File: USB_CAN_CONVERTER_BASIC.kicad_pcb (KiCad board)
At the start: 2 copper layers, 26.6 x 14.9 mm, 24 parts, among them P1 CONN_01X05, P2 CONN_01X02, P3 USB_A, P4 CONN_01X04, U1 STM32F042C6Ux, U2 PSD2CAN, U3 SN65HVD232D, U4 MCP1700T-3302E/TT, U5 USBLC6-2

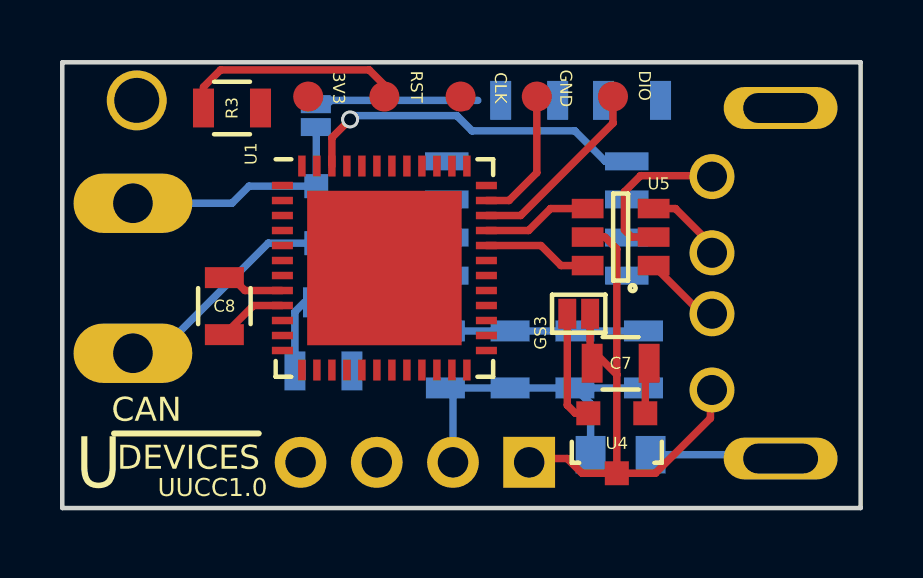
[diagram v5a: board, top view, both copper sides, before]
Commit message: USART change
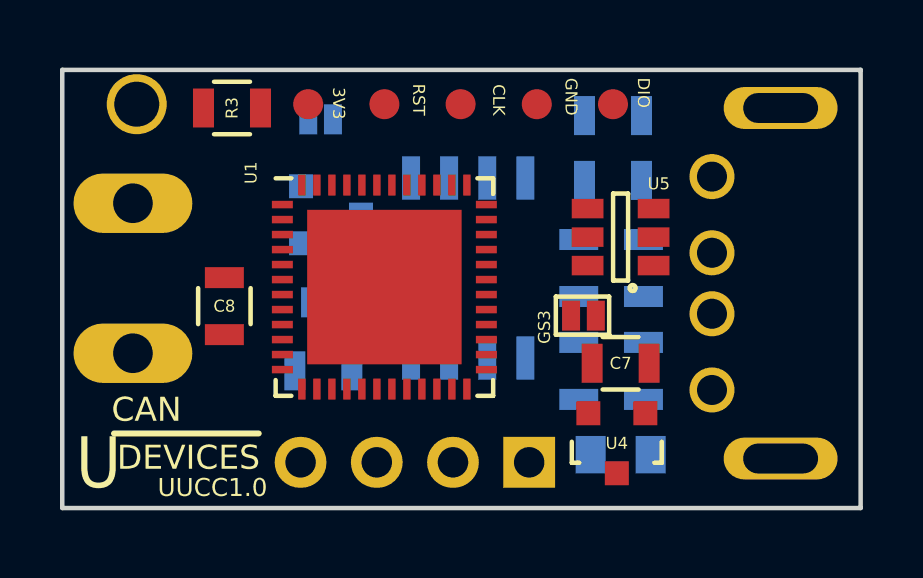
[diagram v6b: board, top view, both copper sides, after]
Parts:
- moved C3 5.39 mm to (157.6, 98.7), turned to 90 degrees
- moved C5 5.39 mm to (159.8, 98.7), turned to 90 degrees
- moved R4 3.86 mm to (158.8, 95.8), turned to 180 degrees
- moved U3 2.82 mm to (153.9, 98.7), turned to 270 degrees
- moved C1 0.81 mm to (158.8, 93.6)
- moved U1 0.63 mm to (151.1, 99.3)
- moved U2 0.51 mm to (149.4, 96.9)
- moved C4 0.40 mm to (157.6, 102.1)
- moved C2 0.38 mm to (159.8, 102.1)
- moved P1 0.25 mm to (152.4, 93.2)
- moved GS1 0.18 mm to (149.0, 93.7), turned to 90 degrees
- moved GS3 0.14 mm to (157.7, 100.3)
- moved REF** 0.13 mm to (142.9, 93.2)
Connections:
- P4 pad 3: /USART1_TX -> /USART_TX
- P4 pad 4: /USART1_RX -> /USART_RX
- U1 pad 1: Net-(U1-Pad1) -> (no net)
- U1 pad 10: Net-(U1-Pad10) -> (no net)
- U1 pad 11: Net-(U1-Pad11) -> (no net)
- U1 pad 12: Net-(U1-Pad12) -> /USART_TX
- U1 pad 13: Net-(U1-Pad13) -> /USART_RX
- U1 pad 14: Net-(U1-Pad14) -> (no net)
- U1 pad 15: Net-(U1-Pad15) -> (no net)
- U1 pad 16: Net-(U1-Pad16) -> (no net)
- U1 pad 17: Net-(U1-Pad17) -> (no net)
- U1 pad 18: Net-(U1-Pad18) -> (no net)
- U1 pad 19: Net-(U1-Pad19) -> (no net)
- U1 pad 2: Net-(U1-Pad2) -> (no net)
- U1 pad 20: Net-(U1-Pad20) -> (no net)
- U1 pad 21: Net-(U1-Pad21) -> (no net)
- U1 pad 22: Net-(U1-Pad22) -> (no net)
- U1 pad 25: Net-(U1-Pad25) -> (no net)
- U1 pad 26: Net-(U1-Pad26) -> (no net)
- U1 pad 27: Net-(U1-Pad27) -> (no net)
- U1 pad 28: Net-(U1-Pad28) -> (no net)
- U1 pad 29: Net-(U1-Pad29) -> (no net)
- U1 pad 3: Net-(U1-Pad3) -> (no net)
- U1 pad 30: /USART1_TX -> (no net)
- U1 pad 31: /USART1_RX -> (no net)
- U1 pad 38: Net-(U1-Pad38) -> (no net)
- U1 pad 39: Net-(U1-Pad39) -> (no net)
- U1 pad 4: Net-(U1-Pad4) -> (no net)
- U1 pad 40: Net-(U1-Pad40) -> (no net)
- U1 pad 41: Net-(U1-Pad41) -> (no net)
- U1 pad 42: Net-(U1-Pad42) -> (no net)
- U1 pad 43: Net-(U1-Pad43) -> (no net)
- U1 pad 44: Net-(U1-Pad44) -> (no net)
- U1 pad 6: Net-(U1-Pad6) -> (no net)
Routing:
- net GND: track 25.7 -> 0.00 mm
- net +5V: track 19.5 -> 0.00 mm
- net +3V3: track 12.6 -> 0.00 mm
- net CAN_TX: track 11.7 -> 0.00 mm, vias 1 -> 0
- net Net-(GS2-Pad2): track 10.0 -> 0.00 mm
- net Net-(GS1-Pad2): track 8.18 -> 0.00 mm
- net Net-(P1-Pad2): track 7.69 -> 0.00 mm
- net SW_DIO: track 6.26 -> 0.00 mm
- net Net-(GS1-Pad1): track 5.45 -> 0.00 mm
- net Net-(L1-Pad2): track 4.32 -> 0.00 mm
- net Net-(U1-Pad33): track 3.68 -> 0.00 mm
- net Net-(U1-Pad32): track 3.65 -> 0.00 mm
- net Net-(P3-Pad3): track 2.65 -> 0.00 mm
- net Net-(P3-Pad2): track 2.55 -> 0.00 mm
- net Net-(GS2-Pad1): track 2.42 -> 0.00 mm
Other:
- board size 26.6 x 14.9 mm -> 26.6 x 14.6 mm

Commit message: Board rooting done.
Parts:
- moved C5 8.56 mm to (151.9, 102.2), turned to 270 degrees
- moved R4 7.09 mm to (152.1, 93.3), turned to 0 degrees
- moved C3 4.89 mm to (154.2, 102.2), turned to 270 degrees
- moved U3 2.69 mm to (156.3, 97.4), turned to 180 degrees
- moved R3 2.36 mm to (145.9, 95.7), turned to 90 degrees
- moved C1 1.30 mm to (157.5, 93.3)
- moved C8 1.25 mm to (145.8, 101.2)
- moved GS3 0.46 mm to (157.3, 100.3)
- moved U2 0.45 mm to (149.0, 97.2), turned to 270 degrees
- moved U5 0.42 mm to (158.7, 97.9)
- moved GS1 0.42 mm to (148.7, 93.4)
- moved P1 0.15 mm to (152.4, 93.4)
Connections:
- REF** pad 1: (no net) -> GND
- U1 pad 1: (no net) -> Net-(U1-Pad1)
- U1 pad 10: (no net) -> Net-(U1-Pad10)
- U1 pad 11: (no net) -> Net-(U1-Pad11)
- U1 pad 14: (no net) -> Net-(U1-Pad14)
- U1 pad 15: (no net) -> Net-(U1-Pad15)
- U1 pad 16: (no net) -> Net-(U1-Pad16)
- U1 pad 17: (no net) -> Net-(U1-Pad17)
- U1 pad 18: (no net) -> Net-(U1-Pad18)
- U1 pad 19: (no net) -> Net-(U1-Pad19)
- U1 pad 2: (no net) -> Net-(U1-Pad2)
- U1 pad 20: (no net) -> Net-(U1-Pad20)
- U1 pad 21: (no net) -> Net-(U1-Pad21)
- U1 pad 22: (no net) -> Net-(U1-Pad22)
- U1 pad 25: (no net) -> Net-(U1-Pad25)
- U1 pad 26: (no net) -> Net-(U1-Pad26)
- U1 pad 27: (no net) -> Net-(U1-Pad27)
- U1 pad 28: (no net) -> Net-(U1-Pad28)
- U1 pad 29: (no net) -> Net-(U1-Pad29)
- U1 pad 3: (no net) -> Net-(U1-Pad3)
- U1 pad 30: (no net) -> Net-(U1-Pad30)
- U1 pad 31: (no net) -> Net-(U1-Pad31)
- U1 pad 38: (no net) -> Net-(U1-Pad38)
- U1 pad 39: (no net) -> Net-(U1-Pad39)
- U1 pad 4: (no net) -> Net-(U1-Pad4)
- U1 pad 40: (no net) -> Net-(U1-Pad40)
- U1 pad 41: (no net) -> Net-(U1-Pad41)
- U1 pad 42: (no net) -> Net-(U1-Pad42)
- U1 pad 43: (no net) -> Net-(U1-Pad43)
- U1 pad 44: (no net) -> Net-(U1-Pad44)
- U1 pad 6: (no net) -> Net-(U1-Pad6)
- U2 pad 1: Net-(GS2-Pad2) -> Net-(GS1-Pad2)
- U2 pad 2: Net-(GS1-Pad2) -> Net-(GS2-Pad2)
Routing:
- net GND: track 0.00 -> 105.3 mm, vias 0 -> 1
- net +3V3: track 0.00 -> 53.9 mm, vias 0 -> 5
- net Net-(C1-Pad2): track 0.00 -> 32.0 mm, vias 0 -> 2
- net CAN_MOD: track 0.00 -> 18.5 mm, vias 0 -> 1
- net +5V: track 0.00 -> 17.9 mm
- net Net-(GS2-Pad2): track 0.00 -> 16.7 mm
- net Net-(L1-Pad2): track 0.00 -> 16.0 mm
- net Net-(GS1-Pad2): track 0.00 -> 14.6 mm
- net Net-(P1-Pad2): track 0.00 -> 14.3 mm
- net CAN_RX: track 0.00 -> 12.3 mm, vias 0 -> 1
- net CAN_TX: track 0.00 -> 11.5 mm, vias 0 -> 1
- net /USART_TX: track 0.00 -> 9.65 mm
- net SW_DIO: track 0.00 -> 6.44 mm
- net Net-(U1-Pad33): track 0.00 -> 3.51 mm
- net Net-(U1-Pad32): track 0.00 -> 3.21 mm
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- added copper zone on B.Cu, net GND
- added copper zone on F.Cu, net GND

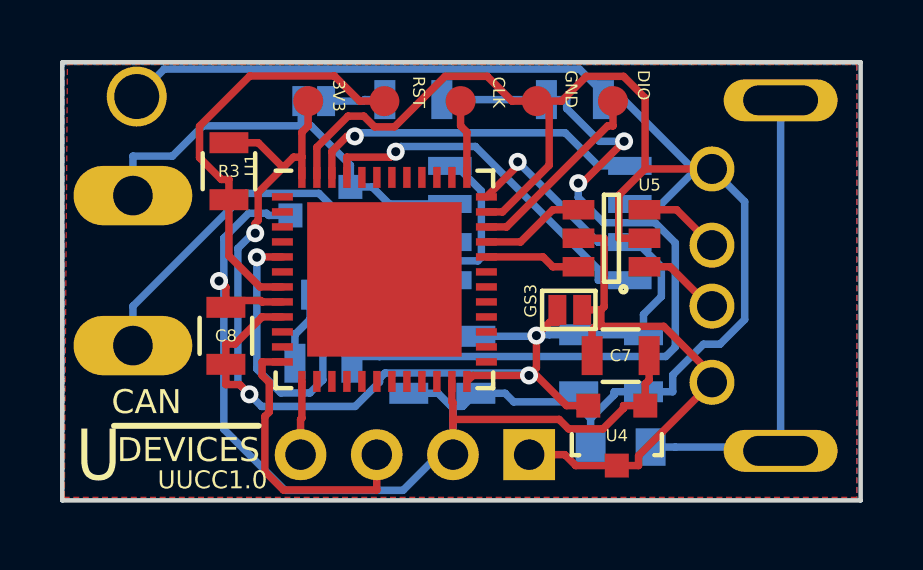
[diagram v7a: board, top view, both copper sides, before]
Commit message: Thermal pad update
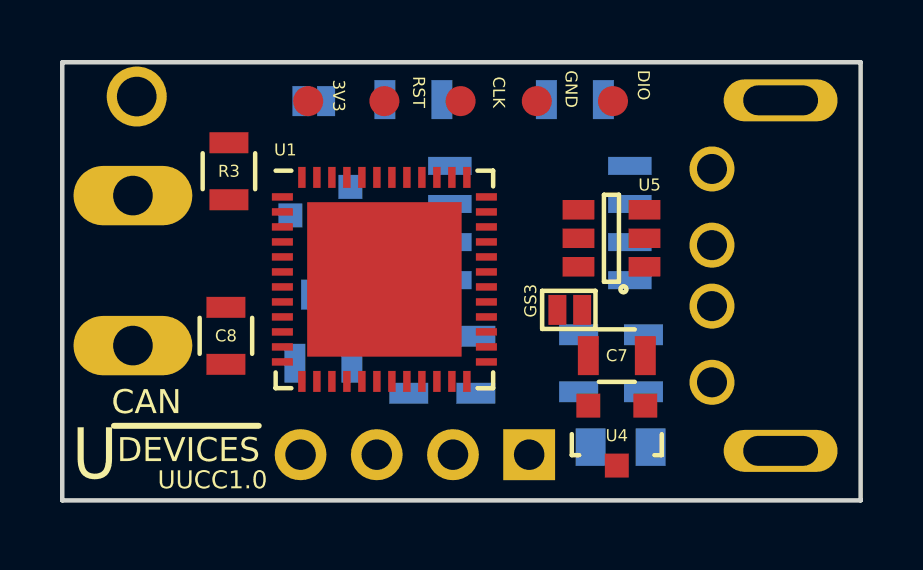
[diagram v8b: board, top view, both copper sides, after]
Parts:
- moved C7 0.13 mm to (158.9, 101.9)
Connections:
- U1 pad 49: (no net) -> GND
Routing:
- net GND: track 105.3 -> 0.00 mm, vias 1 -> 0
- net +3V3: track 53.9 -> 0.00 mm, vias 5 -> 0
- net Net-(C1-Pad2): track 32.0 -> 0.00 mm, vias 2 -> 0
- net CAN_MOD: track 18.5 -> 0.00 mm, vias 1 -> 0
- net +5V: track 17.9 -> 0.00 mm
- net Net-(GS2-Pad2): track 16.7 -> 0.00 mm
- net Net-(L1-Pad2): track 16.0 -> 0.00 mm
- net Net-(GS1-Pad2): track 14.6 -> 0.00 mm
- net Net-(P1-Pad2): track 14.3 -> 0.00 mm
- net CAN_RX: track 12.3 -> 0.00 mm, vias 1 -> 0
- net CAN_TX: track 11.5 -> 0.00 mm, vias 1 -> 0
- net /USART_TX: track 9.65 -> 0.00 mm
- net SW_DIO: track 6.44 -> 0.00 mm
- net Net-(U1-Pad33): track 3.51 -> 0.00 mm
- net Net-(U1-Pad32): track 3.21 -> 0.00 mm
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- removed copper zone on B.Cu, net GND
- removed copper zone on F.Cu, net GND
